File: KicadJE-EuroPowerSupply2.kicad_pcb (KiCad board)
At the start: 2 copper layers, 159 x 128 mm, 141 parts, among them J101 Laptop Power, J102 +-15V thru, J103 +-12v out, J104 +5V out, J105 Laptop Power Out, J106 FrontInterConnVin, J107 FrontInterConnVin, J108 Conn_01x08, J109 Conn_01x08, P101 Doepfer_Power_10pin, P102 Doepfer_Power_16pin, P105 Doepfer_Power_10pin, P106 Doepfer_Power_16pin, Q201 TIP41, Q202 TIP41, Q203 TIP42, Q204 MMBT2907A, Q205 MMBT2222A, Q206 MMBT2907A, SW101 SW_SPDT, U201 LM7812_TO220, U202 LM7805_TO220, U203 Step Down Module +15 to 7v - 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, U204 LM7912_TO220, U205 XL6009 Module DCDC 19 to 30v, U206 TL071, U207 LM78M05_TO252, U208 LM78M12_TO252, U209 MC79M12_TO252

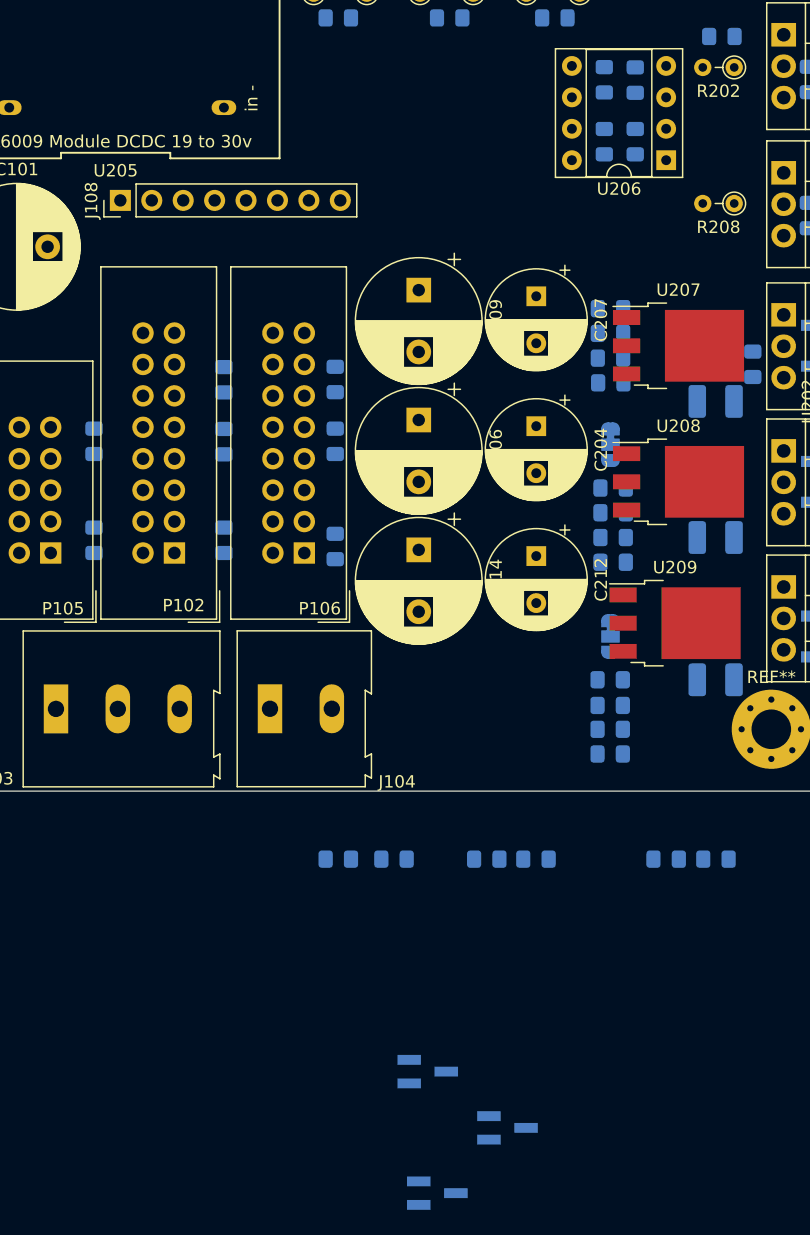
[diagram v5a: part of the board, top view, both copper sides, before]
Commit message: Update KicadJE-EuroPowerSupply2.kicad_pcb
Components placed
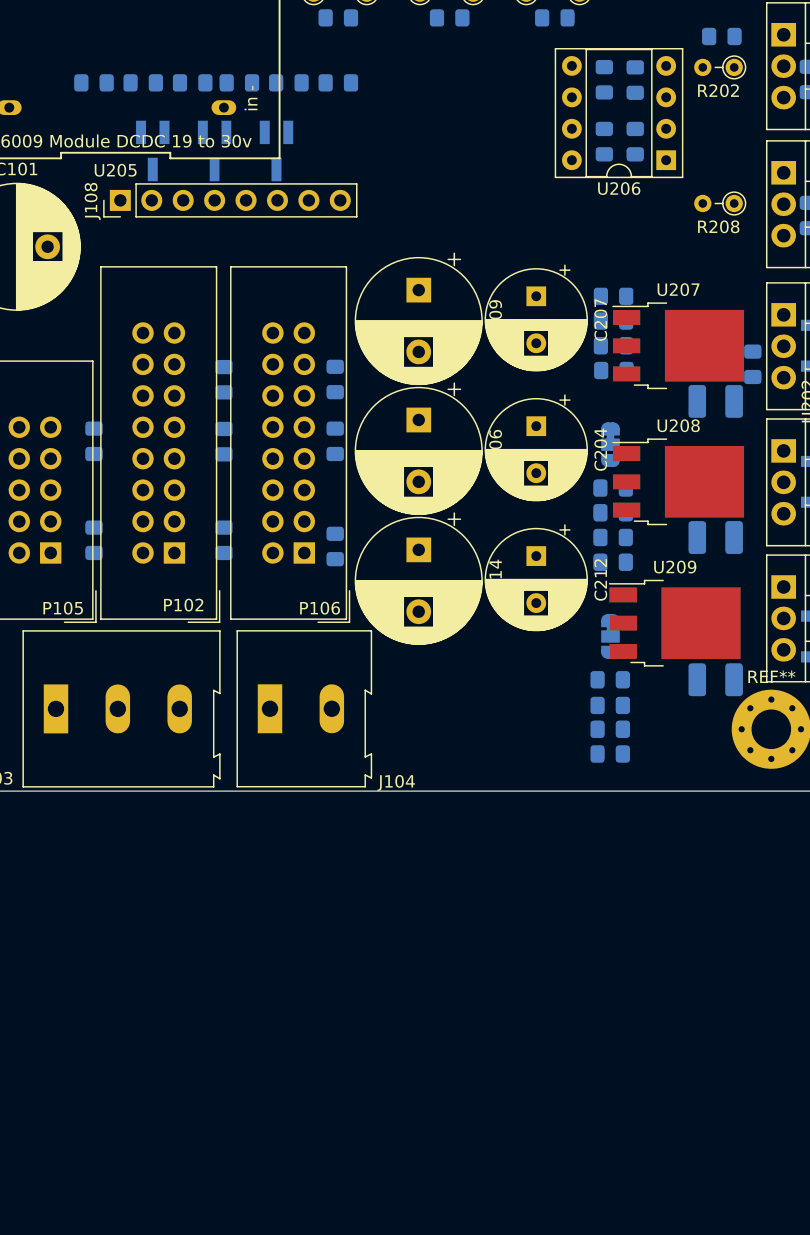
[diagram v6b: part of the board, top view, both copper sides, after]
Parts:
- moved Q204 87.3 mm to (96.0, 98.2), turned to 270 degrees
- moved Q206 82.4 mm to (101.0, 98.2), turned to 270 degrees
- moved Q205 75.4 mm to (106.0, 98.2), turned to 270 degrees
- moved R234 73.6 mm to (103.0, 92.8)
- moved R235 73.5 mm to (99.2, 92.8)
- moved R221 70.3 mm to (95.2, 92.8)
- moved R222 70.3 mm to (91.2, 92.8)
- moved R224 62.9 mm to (111.0, 92.8)
- moved R223 62.9 mm to (107.0, 92.8)
- moved R229 1.03 mm to (133.2, 112.0)
- moved R230 1.03 mm to (133.2, 110.0)
- moved R231 1.03 mm to (133.2, 114.0)
- moved R232 1.03 mm to (133.3, 116.0)
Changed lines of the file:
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@@
   )
   (module Resistor_SMD:R_0805_2012Metric_Pad1.15x1.40mm_HandSolder (layer B.Cu)
-    (at 126.975 155.5)
+    (at 95.225 92.75)
     (descr "Resistor SMD 0805 (2012 Metric), square (rectangular) end terminal, IPC_7351 nominal with elongated pad for handsoldering. (Body size source: https://docs.google.com/spreadsheets/d/1BsfQQcO9C6DZCsRaXUlFlo91Tg2WpOkGARC1WS5S8t0/edit?usp=sharing), generated with kicad-footprint-generator")
     (tags "resistor handsolder")
@@
   )
   (module Resistor_SMD:R_0805_2012Metric_Pad1.15x1.40mm_HandSolder (layer B.Cu)
-    (at 123 155.5 180)
+    (at 91.25 92.75 180)
     (descr "Resistor SMD 0805 (2012 Metric), square (rectangular) end terminal, IPC_7351 nominal with elongated pad for handsoldering. (Body size source: https://docs.google.com/spreadsheets/d/1BsfQQcO9C6DZCsRaXUlFlo91Tg2WpOkGARC1WS5S8t0/edit?usp=sharing), generated with kicad-footprint-generator")
     (tags "resistor handsolder")
@@
   )
   (module Resistor_SMD:R_0805_2012Metric_Pad1.15x1.40mm_HandSolder (layer B.Cu)
-    (at 111 155.5)
+    (at 107 92.75)
     (descr "Resistor SMD 0805 (2012 Metric), square (rectangular) end terminal, IPC_7351 nominal with elongated pad for handsoldering. (Body size source: https://docs.google.com/spreadsheets/d/1BsfQQcO9C6DZCsRaXUlFlo91Tg2WpOkGARC1WS5S8t0/edit?usp=sharing), generated with kicad-footprint-generator")
     (tags "resistor handsolder")
@@
   )
   (module Resistor_SMD:R_0805_2012Metric_Pad1.15x1.40mm_HandSolder (layer B.Cu)
-    (at 115.5 155.5 180)
+    (at 111 92.75 180)
     (descr "Resistor SMD 0805 (2012 Metric), square (rectangular) end terminal, IPC_7351 nominal with elongated pad for handsoldering. (Body size source: https://docs.google.com/spreadsheets/d/1BsfQQcO9C6DZCsRaXUlFlo91Tg2WpOkGARC1WS5S8t0/edit?usp=sharing), generated with kicad-footprint-generator")
     (tags "resistor handsolder")
@@
   )
   (module Resistor_SMD:R_0805_2012Metric_Pad1.15x1.40mm_HandSolder (layer B.Cu)
-    (at 133 113)
+    (at 133.25 112)
     (descr "Resistor SMD 0805 (2012 Metric), square (rectangular) end terminal, IPC_7351 nominal with elongated pad for handsoldering. (Body size source: https://docs.google.com/spreadsheets/d/1BsfQQcO9C6DZCsRaXUlFlo91Tg2WpOkGARC1WS5S8t0/edit?usp=sharing), generated with kicad-footprint-generator")
     (tags "resistor handsolder")
@@
   )
   (module Resistor_SMD:R_0805_2012Metric_Pad1.15x1.40mm_HandSolder (layer B.Cu)
-    (at 133 111)
+    (at 133.25 110)
     (descr "Resistor SMD 0805 (2012 Metric), square (rectangular) end terminal, IPC_7351 nominal with elongated pad for handsoldering. (Body size source: https://docs.google.com/spreadsheets/d/1BsfQQcO9C6DZCsRaXUlFlo91Tg2WpOkGARC1WS5S8t0/edit?usp=sharing), generated with kicad-footprint-generator")
     (tags "resistor handsolder")
@@
   )
   (module Resistor_SMD:R_0805_2012Metric_Pad1.15x1.40mm_HandSolder (layer B.Cu)
-    (at 133 115)
+    (at 133.25 114)
     (descr "Resistor SMD 0805 (2012 Metric), square (rectangular) end terminal, IPC_7351 nominal with elongated pad for handsoldering. (Body size source: https://docs.google.com/spreadsheets/d/1BsfQQcO9C6DZCsRaXUlFlo91Tg2WpOkGARC1WS5S8t0/edit?usp=sharing), generated with kicad-footprint-generator")
     (tags "resistor handsolder")
@@
   )
   (module Resistor_SMD:R_0805_2012Metric_Pad1.15x1.40mm_HandSolder (layer B.Cu)
-    (at 133.025 117)
+    (at 133.275 116)
     (descr "Resistor SMD 0805 (2012 Metric), square (rectangular) end terminal, IPC_7351 nominal with elongated pad for handsoldering. (Body size source: https://docs.google.com/spreadsheets/d/1BsfQQcO9C6DZCsRaXUlFlo91Tg2WpOkGARC1WS5S8t0/edit?usp=sharing), generated with kicad-footprint-generator")
     (tags "resistor handsolder")
@@
   )
   (module Resistor_SMD:R_0805_2012Metric_Pad1.15x1.40mm_HandSolder (layer B.Cu)
-    (at 141.525 155.5)
+    (at 103 92.75)
     (descr "Resistor SMD 0805 (2012 Metric), square (rectangular) end terminal, IPC_7351 nominal with elongated pad for handsoldering. (Body size source: https://docs.google.com/spreadsheets/d/1BsfQQcO9C6DZCsRaXUlFlo91Tg2WpOkGARC1WS5S8t0/edit?usp=sharing), generated with kicad-footprint-generator")
     (tags "resistor handsolder")
@@
   )
   (module Resistor_SMD:R_0805_2012Metric_Pad1.15x1.40mm_HandSolder (layer B.Cu)
-    (at 137.5 155.5 180)
+    (at 99.225 92.75 180)
     (descr "Resistor SMD 0805 (2012 Metric), square (rectangular) end terminal, IPC_7351 nominal with elongated pad for handsoldering. (Body size source: https://docs.google.com/spreadsheets/d/1BsfQQcO9C6DZCsRaXUlFlo91Tg2WpOkGARC1WS5S8t0/edit?usp=sharing), generated with kicad-footprint-generator")
     (tags "resistor handsolder")
@@
   )
   (module Package_TO_SOT_SMD:SOT-23_Handsoldering (layer B.Cu)
-    (at 119 182.5)
+    (at 96 98.25 270)
     (descr "SOT-23, Handsoldering")
     (tags SOT-23)
     (attr smd)
-    (fp_text reference Q204 (at 0 2.5) (layer B.SilkS)
-      (effects (font (size 1 1) (thickness 0.15)) (justify mirror))
-    )
-    (fp_text value MMBT2907A (at 0 -2.5) (layer B.Fab)
+    (fp_text reference Q204 (at 0 2.5 90) (layer B.SilkS)
+      (effects (font (size 1 1) (thickness 0.15)) (justify mirror))
+    )
+    (fp_text value MMBT2907A (at 0 -2.5 90) (layer B.Fab)
       (effects (font (size 1 1) (thickness 0.15)) (justify mirror))
     )
@@
     (fp_line (start 0.76 1.58) (end 0.76 0.65) (layer B.SilkS) (width 0.12))
     (fp_line (start 0.76 -1.58) (end 0.76 -0.65) (layer B.SilkS) (width 0.12))
-    (fp_text user %R (at 0 0 -90) (layer B.Fab)
+    (fp_text user %R (at 0 0 180) (layer B.Fab)
       (effects (font (size 0.5 0.5) (thickness 0.075)) (justify mirror))
     )
-    (pad 3 smd rect (at 1.5 0) (size 1.9 0.8) (layers B.Cu B.Paste B.Mask)
+    (pad 3 smd rect (at 1.5 0 270) (size 1.9 0.8) (layers B.Cu B.Paste B.Mask)
       (net 53 I+12))
-    (pad 2 smd rect (at -1.5 -0.95) (size 1.9 0.8) (layers B.Cu B.Paste B.Mask)
+    (pad 2 smd rect (at -1.5 -0.95 270) (size 1.9 0.8) (layers B.Cu B.Paste B.Mask)
       (net 47 "Net-(JP201-Pad2)"))
-    (pad 1 smd rect (at -1.5 0.95) (size 1.9 0.8) (layers B.Cu B.Paste B.Mask)
+    (pad 1 smd rect (at -1.5 0.95 270) (size 1.9 0.8) (layers B.Cu B.Paste B.Mask)
       (net 50 /VoltageRegulation/b4))
     (model ${KISYS3DMOD}/Package_TO_SOT_SMD.3dshapes/SOT-23.wrl
@@
   )
   (module Package_TO_SOT_SMD:SOT-23_Handsoldering (layer B.Cu)
-    (at 118.225001 172.674999)
+    (at 106 98.25 270)
     (descr "SOT-23, Handsoldering")
     (tags SOT-23)
     (attr smd)
-    (fp_text reference Q205 (at 0 2.5) (layer B.SilkS)
-      (effects (font (size 1 1) (thickness 0.15)) (justify mirror))
-    )
-    (fp_text value MMBT2222A (at 0 -2.5) (layer B.Fab)
-      (effects (font (size 1 1) (thickness 0.15)) (justify mirror))
-    )
-    (fp_text user %R (at 0 0 -90) (layer B.Fab)
+    (fp_text reference Q205 (at 0 2.5 90) (layer B.SilkS)
+      (effects (font (size 1 1) (thickness 0.15)) (justify mirror))
+    )
+    (fp_text value MMBT2222A (at 0 -2.5 90) (layer B.Fab)
+      (effects (font (size 1 1) (thickness 0.15)) (justify mirror))
+    )
+    (fp_text user %R (at 0 0 180) (layer B.Fab)
       (effects (font (size 0.5 0.5) (thickness 0.075)) (justify mirror))
     )
@@
     (fp_line (start -0.7 -1.52) (end 0.7 -1.52) (layer B.Fab) (width 0.1))
     (fp_line (start 0.76 -1.58) (end -0.7 -1.58) (layer B.SilkS) (width 0.12))
-    (pad 1 smd rect (at -1.5 0.95) (size 1.9 0.8) (layers B.Cu B.Paste B.Mask)
+    (pad 1 smd rect (at -1.5 0.95 270) (size 1.9 0.8) (layers B.Cu B.Paste B.Mask)
       (net 49 /VoltageRegulation/b5))
-    (pad 2 smd rect (at -1.5 -0.95) (size 1.9 0.8) (layers B.Cu B.Paste B.Mask)
+    (pad 2 smd rect (at -1.5 -0.95 270) (size 1.9 0.8) (layers B.Cu B.Paste B.Mask)
       (net 48 "Net-(JP202-Pad2)"))
-    (pad 3 smd rect (at 1.5 0) (size 1.9 0.8) (layers B.Cu B.Paste B.Mask)
+    (pad 3 smd rect (at 1.5 0 270) (size 1.9 0.8) (layers B.Cu B.Paste B.Mask)
       (net 52 I-12))
     (model ${KISYS3DMOD}/Package_TO_SOT_SMD.3dshapes/SOT-23.wrl
@@
   )
   (module Package_TO_SOT_SMD:SOT-23_Handsoldering (layer B.Cu)
-    (at 124.675001 177.224999)
+    (at 101 98.25 270)
     (descr "SOT-23, Handsoldering")
     (tags SOT-23)
     (attr smd)
-    (fp_text reference Q206 (at 0 2.5) (layer B.SilkS)
-      (effects (font (size 1 1) (thickness 0.15)) (justify mirror))
-    )
-    (fp_text value MMBT2907A (at 0 -2.5) (layer B.Fab)
-      (effects (font (size 1 1) (thickness 0.15)) (justify mirror))
-    )
-    (fp_text user %R (at 0 0 -90) (layer B.Fab)
+    (fp_text reference Q206 (at 0 2.5 90) (layer B.SilkS)
+      (effects (font (size 1 1) (thickness 0.15)) (justify mirror))
+    )
+    (fp_text value MMBT2907A (at 0 -2.5 90) (layer B.Fab)
+      (effects (font (size 1 1) (thickness 0.15)) (justify mirror))
+    )
+    (fp_text user %R (at 0 0 180) (layer B.Fab)
       (effects (font (size 0.5 0.5) (thickness 0.075)) (justify mirror))
     )
@@
     (fp_line (start -0.7 -1.52) (end 0.7 -1.52) (layer B.Fab) (width 0.1))
     (fp_line (start 0.76 -1.58) (end -0.7 -1.58) (layer B.SilkS) (width 0.12))
-    (pad 1 smd rect (at -1.5 0.95) (size 1.9 0.8) (layers B.Cu B.Paste B.Mask)
+    (pad 1 smd rect (at -1.5 0.95 270) (size 1.9 0.8) (layers B.Cu B.Paste B.Mask)
       (net 51 "Net-(Q206-Pad1)"))
-    (pad 2 smd rect (at -1.5 -0.95) (size 1.9 0.8) (layers B.Cu B.Paste B.Mask)
+    (pad 2 smd rect (at -1.5 -0.95 270) (size 1.9 0.8) (layers B.Cu B.Paste B.Mask)
       (net 14 5Vreg))
-    (pad 3 smd rect (at 1.5 0) (size 1.9 0.8) (layers B.Cu B.Paste B.Mask)
+    (pad 3 smd rect (at 1.5 0 270) (size 1.9 0.8) (layers B.Cu B.Paste B.Mask)
       (net 54 I+5))
     (model ${KISYS3DMOD}/Package_TO_SOT_SMD.3dshapes/SOT-23.wrl

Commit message: Board setup - power lines
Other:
- net class Default: trace_width 0.15 -> 0.25
- net class Power: trace_width 0.4 -> 0.6
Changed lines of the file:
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@@
   )
   (page A4)
+  (title_block
+    (title "Euro Power Supply Mk2")
+    (date 2020-03-16)
+    (rev "Rev A")
+    (company "Johansen Engineering")
+  )
   (layers
     (0 F.Cu signal)
@@
   )
   (setup
-    (last_trace_width 0.15)
+    (last_trace_width 0.25)
     (trace_clearance 0.15)
     (zone_clearance 0.508)
@@
   (net_class Default "This is the default net class."
     (clearance 0.15)
-    (trace_width 0.15)
+    (trace_width 0.25)
     (via_dia 0.7)
     (via_drill 0.4)
     (uvia_dia 0.3)
     (uvia_drill 0.1)
-    (add_net +12V)
-    (add_net +15V)
-    (add_net +7.5V)
-    (add_net -12V)
-    (add_net -12Vreg)
-    (add_net -15V)
-    (add_net /DCSleeve)
-    (add_net /VoltageRegulation/7V)
-    (add_net /VoltageRegulation/GND-7V)
     (add_net /VoltageRegulation/b4)
     (add_net /VoltageRegulation/b5)
-    (add_net 12Vreg)
-    (add_net 5Vreg)
     (add_net CV)
-    (add_net DCDC+)
     (add_net Gate)
     (add_net I+12)
@@
     (add_net "Net-(R201-Pad1)")
     (add_net "Net-(R206-Pad2)")
+  )
+  (net_class Power ""
+    (clearance 0.2)
+    (trace_width 0.6)
+    (via_dia 0.8)
+    (via_drill 0.4)
+    (uvia_dia 0.3)
+    (uvia_drill 0.1)
+    (add_net +12V)
+    (add_net +15V)
+    (add_net +5V)
+    (add_net +7.5V)
+    (add_net -12V)
+    (add_net -12Vreg)
+    (add_net -15V)
+    (add_net /DCSleeve)
+    (add_net /VoltageRegulation/7V)
+    (add_net /VoltageRegulation/GND-7V)
+    (add_net 12Vreg)
+    (add_net 5Vreg)
+    (add_net DCDC+)
+    (add_net GND)
     (add_net Vin+15)
     (add_net Vin-15)
@@
     (add_net VinGND)
   )
-  (net_class Power ""
-    (clearance 0.2)
-    (trace_width 0.4)
-    (via_dia 0.8)
-    (via_drill 0.4)
-    (uvia_dia 0.3)
-    (uvia_drill 0.1)
-    (add_net +5V)
-    (add_net GND)
-  )
   (module AJ:Jack_6m3 (layer F.Cu)

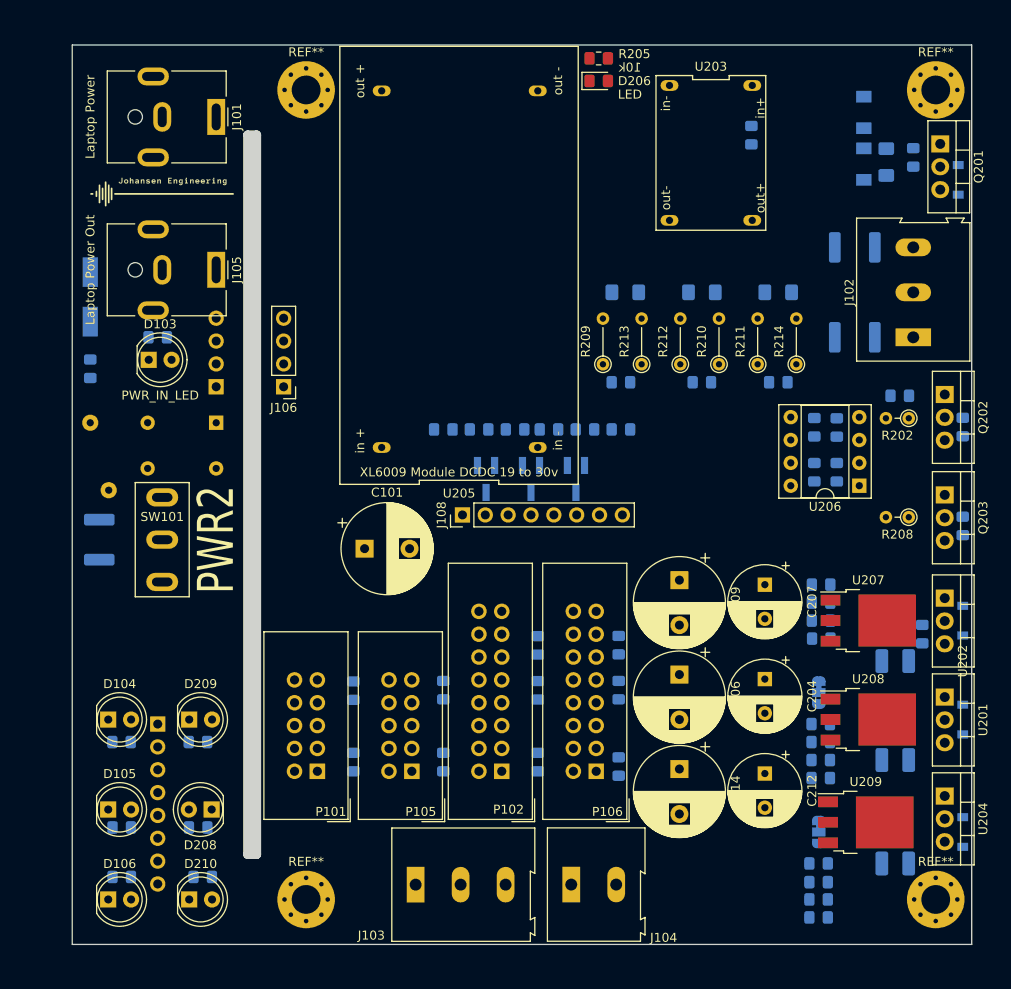
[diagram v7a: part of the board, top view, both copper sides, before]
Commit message: Update KicadJE-EuroPowerSupply2.kicad_pcb
Wired initially
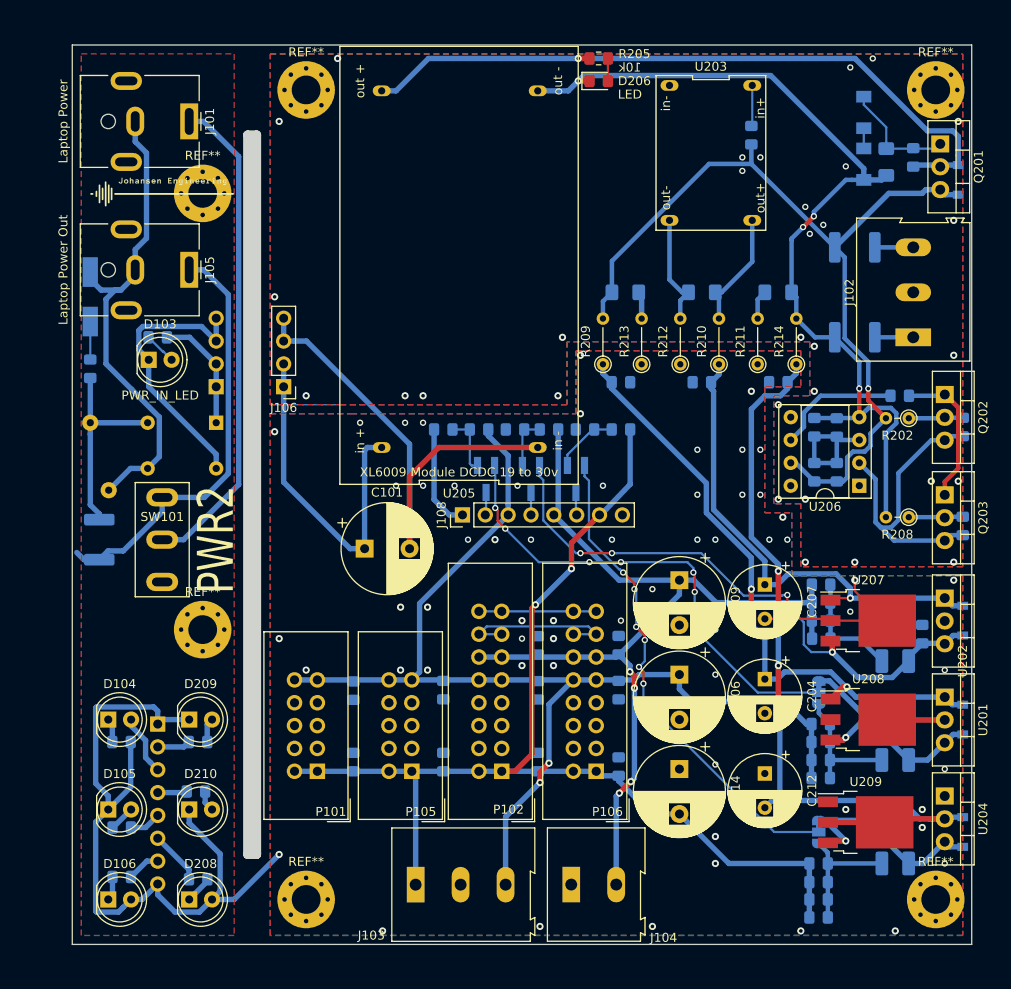
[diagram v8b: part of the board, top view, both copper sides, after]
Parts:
- added REF**: MountingHole_3.2mm_M3_Pad_Via, MountingHole:MountingHole_3.2mm_M3_Pad_Via, F.Cu at (64.5, 115.0)
- added REF**: MountingHole_3.2mm_M3_Pad_Via, MountingHole:MountingHole_3.2mm_M3_Pad_Via, F.Cu at (64.5, 66.5)
- moved D208 10.3 mm to (63.0, 145.0), turned to 0 degrees
- moved D210 10.0 mm to (63.0, 135.0)
- moved R233 9.53 mm to (63.8, 133.0)
- moved R216 5.75 mm to (64.0, 142.8)
- moved J101 3.04 mm to (63.0, 58.5)
- moved J105 3.00 mm to (63.0, 75.0)
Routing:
- net +12V: track 0.00 -> 132.8 mm, vias 0 -> 2
- net -12V: track 0.00 -> 129.2 mm, vias 0 -> 2
- net GND: track 0.00 -> 120.7 mm, vias 0 -> 62
- net +5V: track 0.00 -> 105.9 mm, vias 0 -> 4
- net Vin-15: track 0.00 -> 103.6 mm, vias 0 -> 4
- net Vin+15: track 0.00 -> 96.5 mm, vias 0 -> 1
- net -15V: track 0.00 -> 89.6 mm, vias 0 -> 4
- net Vin-Neg19: track 0.00 -> 87.4 mm
- net DCDC+: track 0.00 -> 78.7 mm, vias 0 -> 1
- net +15V: track 0.00 -> 68.8 mm, vias 0 -> 3
- net 5Vreg: track 0.00 -> 66.2 mm, vias 0 -> 5
- net Net-(JP202-Pad2): track 0.00 -> 55.0 mm, vias 0 -> 6
- net Net-(J101-Pad1): track 0.00 -> 54.6 mm
- net /DCSleeve: track 0.00 -> 54.4 mm
- net +7.5V: track 0.00 -> 54.2 mm, vias 0 -> 1
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- added copper zone on B.Cu, net VinGND
- added copper zone on F.Cu, net VinGND
